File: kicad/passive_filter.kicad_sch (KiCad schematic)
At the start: 3 parts, among them J11 Conn_01x03

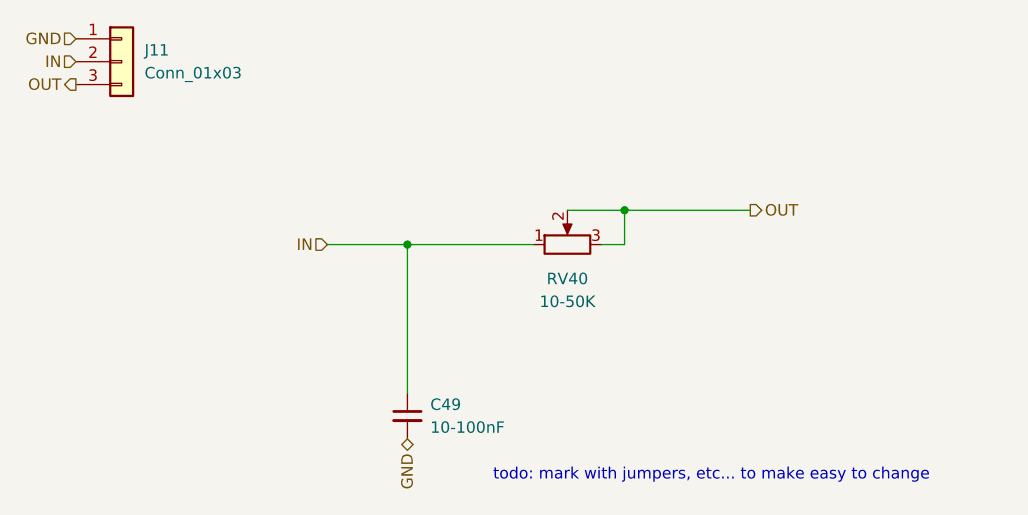
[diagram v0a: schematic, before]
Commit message: mark components as DNP, add LCSC part numbers
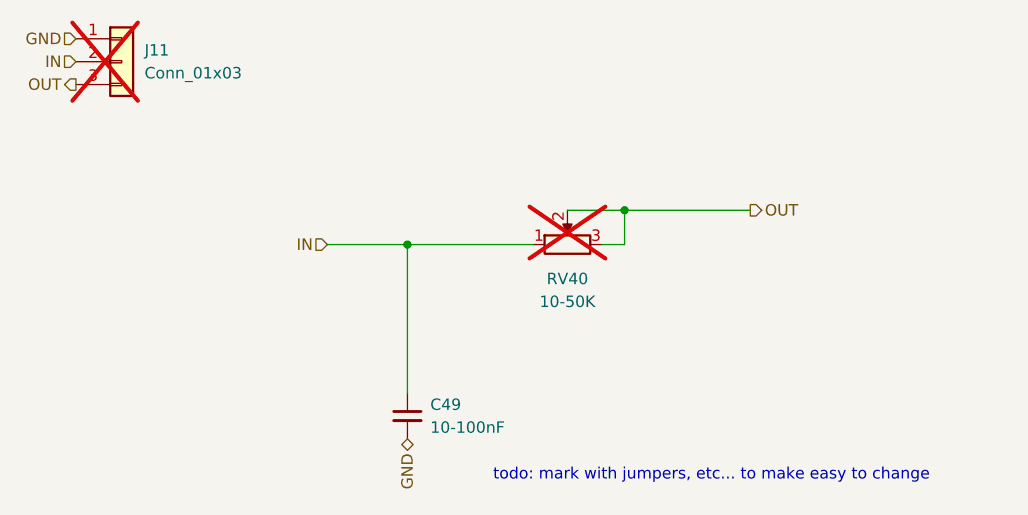
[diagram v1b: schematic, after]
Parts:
- J11, RV40: now not fitted
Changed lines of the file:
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@@
+			)
+		)
+		(property "LCSC Part" ""
+			(at 77.47 77.47 0)
+			(effects
+				(font
+					(size 1.27 1.27)
+				)
+				(hide yes)
 			)
 		)
@@
 		(in_bom yes)
 		(on_board yes)
-		(dnp no)
+		(dnp yes)
 		(fields_autoplaced yes)
 		(property "Reference" "RV40"
@@
 			)
 		)
+		(property "LCSC Part" ""
+			(at 95.25 58.42 0)
+			(effects
+				(font
+					(size 1.27 1.27)
+				)
+				(hide yes)
+			)
+		)
 		(pin "2"
 		)
@@
 		(in_bom yes)
 		(on_board yes)
-		(dnp no)
+		(dnp yes)
 		(fields_autoplaced yes)
 		(property "Reference" "J11"
@@
 			(at 45.72 38.1 0)
 			(effects
+				(font
+					(size 1.27 1.27)
+				)
+				(hide yes)
+			)
+		)
+		(property "LCSC Part" ""
+			(at 45.72 38.1 0)
+			(effects
